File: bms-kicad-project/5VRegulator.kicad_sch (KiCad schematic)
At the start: 45 parts, among them U6 SIC461ED-T1-GE3

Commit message: feat: schematic pretty much done
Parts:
- removed R111: 0, FixedWing:RC1206N_YAG, symbol FixedWing:RC1206JR-070RL
- added R111: 0, FixedWing:RES_CRCW_0805_VIS, symbol FixedWing:CRCW08050000Z0EA
- added TP16, TP17, TP18: TestPoint, TestPoint:TestPoint_Pad_D1.5mm, symbol Connector:TestPoint
- C40: value 220u -> 220µ
- C43: value 1u -> 1µ
- C45: value 4.7u -> 4.7µ
- C49, R117, R118: now not fitted
- C51, C52, C53, C54, C55, C56, C57, C58, C59, C60, C61, C62, C63, C64: value 47u -> 47µ
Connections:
- net +5V: now also TP18.1
- net at R104.1, R105.2, U6.3 (EN): now also TP16.1
- net at LED14.2 (A), R108.2, U6.2 (PGOOD): now also TP17.1
- net at C43.1, R108.1, U6.26 (VDD): now also R111.1
- net at U6.18 (ULTRASONIC): now also R111.2
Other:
- moved on the sheet: C40, C41, C42, C43, C44, C45, C46, C47, C48, C50, C51, C52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

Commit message: feat: schematic cleanup, continued layout
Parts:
- R110: value 41.2 -> 41.2k
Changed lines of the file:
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@@
   (symbol (lib_id "power:GNDA") (at 49.53 240.03 0) (unit 1)
     (in_bom yes) (on_board yes) (dnp no)
-    (property "Reference" "#PWR051" (at 49.53 246.38 0)
+    (property "Reference" "#PWR052" (at 49.53 246.38 0)
       (effects (font (size 1.27 1.27)) hide)
     )
@@
       (project "bms-board"
         (path "/8a7831d1-a913-4f04-8780-225d2234b41d/9bfcf0e7-ef8d-4492-b04a-6397126b0bad"
-          (reference "#PWR051") (unit 1)
+          (reference "#PWR052") (unit 1)
         )
       )
@@
   (symbol (lib_id "power:GNDA") (at 231.14 201.93 0) (unit 1)
     (in_bom yes) (on_board yes) (dnp no)
-    (property "Reference" "#PWR055" (at 231.14 208.28 0)
+    (property "Reference" "#PWR056" (at 231.14 208.28 0)
       (effects (font (size 1.27 1.27)) hide)
     )
@@
       (project "bms-board"
         (path "/8a7831d1-a913-4f04-8780-225d2234b41d/9bfcf0e7-ef8d-4492-b04a-6397126b0bad"
-          (reference "#PWR055") (unit 1)
+          (reference "#PWR056") (unit 1)
         )
       )
@@
   (symbol (lib_id "power:+5V") (at 318.77 50.8 0) (unit 1)
     (in_bom yes) (on_board yes) (dnp no)
-    (property "Reference" "#PWR057" (at 318.77 54.61 0)
+    (property "Reference" "#PWR058" (at 318.77 54.61 0)
       (effects (font (size 1.27 1.27)) hide)
     )
@@
       (project "bms-board"
         (path "/8a7831d1-a913-4f04-8780-225d2234b41d/9bfcf0e7-ef8d-4492-b04a-6397126b0bad"
-          (reference "#PWR057") (unit 1)
+          (reference "#PWR058") (unit 1)
         )
       )
@@
   (symbol (lib_id "power:GNDPWR") (at 236.22 133.35 0) (unit 1)
     (in_bom yes) (on_board yes) (dnp no)
-    (property "Reference" "#PWR056" (at 236.22 138.43 0)
+    (property "Reference" "#PWR057" (at 236.22 138.43 0)
       (effects (font (size 1.27 1.27)) hide)
     )
@@
       (project "bms-board"
         (path "/8a7831d1-a913-4f04-8780-225d2234b41d/9bfcf0e7-ef8d-4492-b04a-6397126b0bad"
-          (reference "#PWR056") (unit 1)
+          (reference "#PWR057") (unit 1)
         )
       )
@@
   (symbol (lib_id "power:GNDPWR") (at 396.24 210.82 0) (unit 1)
     (in_bom yes) (on_board yes) (dnp no) (fields_autoplaced)
-    (property "Reference" "#PWR060" (at 396.24 215.9 0)
+    (property "Reference" "#PWR061" (at 396.24 215.9 0)
       (effects (font (size 1.27 1.27)) hide)
     )
@@
       (project "bms-board"
         (path "/8a7831d1-a913-4f04-8780-225d2234b41d/9bfcf0e7-ef8d-4492-b04a-6397126b0bad"
-          (reference "#PWR060") (unit 1)
+          (reference "#PWR061") (unit 1)
         )
       )
@@
   (symbol (lib_id "power:GNDPWR") (at 44.45 87.63 0) (unit 1)
     (in_bom yes) (on_board yes) (dnp no) (fields_autoplaced)
-    (property "Reference" "#PWR050" (at 44.45 92.71 0)
+    (property "Reference" "#PWR051" (at 44.45 92.71 0)
       (effects (font (size 1.27 1.27)) hide)
     )
@@
       (project "bms-board"
         (path "/8a7831d1-a913-4f04-8780-225d2234b41d/9bfcf0e7-ef8d-4492-b04a-6397126b0bad"
-          (reference "#PWR050") (unit 1)
+          (reference "#PWR051") (unit 1)
         )
       )
@@
   (symbol (lib_id "power:GNDPWR") (at 64.77 240.03 0) (unit 1)
     (in_bom yes) (on_board yes) (dnp no) (fields_autoplaced)
-    (property "Reference" "#PWR052" (at 64.77 245.11 0)
+    (property "Reference" "#PWR053" (at 64.77 245.11 0)
       (effects (font (size 1.27 1.27)) hide)
     )
@@
       (project "bms-board"
         (path "/8a7831d1-a913-4f04-8780-225d2234b41d/9bfcf0e7-ef8d-4492-b04a-6397126b0bad"
-          (reference "#PWR052") (unit 1)
+          (reference "#PWR053") (unit 1)
         )
       )
@@
       (effects (font (size 1.27 1.27)))
     )
-    (property "Value" "41.2" (at 168.91 170.18 0)
+    (property "Value" "41.2k" (at 168.91 170.18 0)
       (effects (font (size 1.27 1.27)))
     )
@@
   (symbol (lib_id "power:+BATT") (at 44.45 67.31 0) (unit 1)
     (in_bom yes) (on_board yes) (dnp no) (fields_autoplaced)
-    (property "Reference" "#PWR049" (at 44.45 71.12 0)
+    (property "Reference" "#PWR050" (at 44.45 71.12 0)
       (effects (font (size 1.27 1.27)) hide)
     )
@@
       (project "bms-board"
         (path "/8a7831d1-a913-4f04-8780-225d2234b41d/9bfcf0e7-ef8d-4492-b04a-6397126b0bad"
-          (reference "#PWR049") (unit 1)
+          (reference "#PWR050") (unit 1)
         )
       )
@@
   (symbol (lib_id "power:GNDPWR") (at 344.17 171.45 0) (unit 1)
     (in_bom yes) (on_board yes) (dnp no)
-    (property "Reference" "#PWR059" (at 344.17 176.53 0)
+    (property "Reference" "#PWR060" (at 344.17 176.53 0)
       (effects (font (size 1.27 1.27)) hide)
     )
@@
       (project "bms-board"
         (path "/8a7831d1-a913-4f04-8780-225d2234b41d/9bfcf0e7-ef8d-4492-b04a-6397126b0bad"
-          (reference "#PWR059") (unit 1)
+          (reference "#PWR060") (unit 1)
         )
       )
@@
   (symbol (lib_id "power:GNDPWR") (at 87.63 102.87 0) (unit 1)
     (in_bom yes) (on_board yes) (dnp no) (fields_autoplaced)
-    (property "Reference" "#PWR054" (at 87.63 107.95 0)
+    (property "Reference" "#PWR055" (at 87.63 107.95 0)
       (effects (font (size 1.27 1.27)) hide)
     )
@@
       (project "bms-board"
         (path "/8a7831d1-a913-4f04-8780-225d2234b41d/9bfcf0e7-ef8d-4492-b04a-6397126b0bad"
-          (reference "#PWR054") (unit 1)
+          (reference "#PWR055") (unit 1)
         )
       )
@@
   (symbol (lib_id "power:GNDPWR") (at 322.58 115.57 0) (unit 1)
     (in_bom yes) (on_board yes) (dnp no) (fields_autoplaced)
-    (property "Reference" "#PWR058" (at 322.58 120.65 0)
+    (property "Reference" "#PWR059" (at 322.58 120.65 0)
       (effects (font (size 1.27 1.27)) hide)
     )
@@
       (project "bms-board"
         (path "/8a7831d1-a913-4f04-8780-225d2234b41d/9bfcf0e7-ef8d-4492-b04a-6397126b0bad"
-          (reference "#PWR058") (unit 1)
+          (reference "#PWR059") (unit 1)
         )
       )
@@
   (symbol (lib_id "power:GND") (at 80.01 240.03 0) (unit 1)
     (in_bom yes) (on_board yes) (dnp no)
-    (property "Reference" "#PWR053" (at 80.01 246.38 0)
+    (property "Reference" "#PWR054" (at 80.01 246.38 0)
       (effects (font (size 1.27 1.27)) hide)
     )
@@
       (project "bms-board"
         (path "/8a7831d1-a913-4f04-8780-225d2234b41d/9bfcf0e7-ef8d-4492-b04a-6397126b0bad"
-          (reference "#PWR053") (unit 1)
-        )
-      )
+          (reference "#PWR054") (unit 1)
+        )
+      )

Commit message: feat: lotta layout
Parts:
- removed LED14: LTST-C170KGKT, FixedWing:LED_LTST-C170KGKT_LTO, symbol FixedWing:LTST-C170KGKT
- removed R108: 10k, FixedWing:KOA_Speer-RK73H2A-0-0-MFG, symbol FixedWing:RK73H2ATTD1002F
- removed R118: R, Resistor_SMD:R_0805_2012Metric, symbol Device:R
- added C41: 0.1µ, FixedWing:CAP_GCJ-18_MUR, symbol FixedWing:GCJ188R72A104KA01D
- added LED15: LTST-C170KGKT, FixedWing:LED_LTST-C170KGKT_LTO, symbol FixedWing:LTST-C170KGKT
- added R109: 93.1k, FixedWing:RESC2012X60N, symbol FixedWing:RC0805FR-0793K1L
- added R116: 5.1k, FixedWing:RESC2012X60N, symbol FixedWing:RC0805JR-075K1L
- renumbered C40 to C39, C41 to C40, R104 to R105, R105 to R106, R106 to R107, R107 to R108, R109 to R110, R110 to R111, R111 to R112, R112 to R113, R113 to R114, R114 to R115, R115 to R117, R116 to R118, R117 to R119, R119 to R120
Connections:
- net +5V: now also R116.2
- net +BATT: now also C41.2
- net GND: now also LED15.1 (K)
- net GNDPWR: now also C41.1
- net PGOOD: now reaches TP17.1, U6.2 (PGOOD)
- net PGOOD: now also R109.2
- net at C43.1, R112.1, U6.26 (VDD): now also R109.1
- new net: LED15.2 (A), R116.1
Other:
- moved on the sheet: C39, C40, C49, R105, R106, R107, R119

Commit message: feat: big pre-design review schematic commit
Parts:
- renumbered C39 to C28, C40 to C29, C41 to C30, C42 to C31, C43 to C32, C44 to C33, C45 to C34, C46 to C35, C47 to C36, C48 to C37, C49 to C38, C50 to C39, C51 to C40, C52 to C41, C53 to C42, C54 to C43, C55 to C44, C56 to C45, C57 to C46, C58 to C47, C59 to C48, C60 to C49, C61 to C50, C62 to C51, C63 to C52, C64 to C53, LED15 to LED13, R110 to R100, R111 to R101, R112 to R102, R113 to R103, R114 to R104, R115 to R105, R116 to R106, R117 to R107, R118 to R108, R119 to R109, R120 to R110, R105 to R95, R106 to R96, R107 to R97, R108 to R98, R109 to R99, TP16 to TP5, TP17 to TP6, TP18 to TP7, U6 to U3
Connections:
- net PGOOD: now also R99.1; no longer R99.2
- net at C32.1, R102.1, U3.26 (VDD): no longer R99.1
- new net +3V3: R99.2
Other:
- company: (none) -> AeroNU - FixedWing
- moved on the sheet: R99

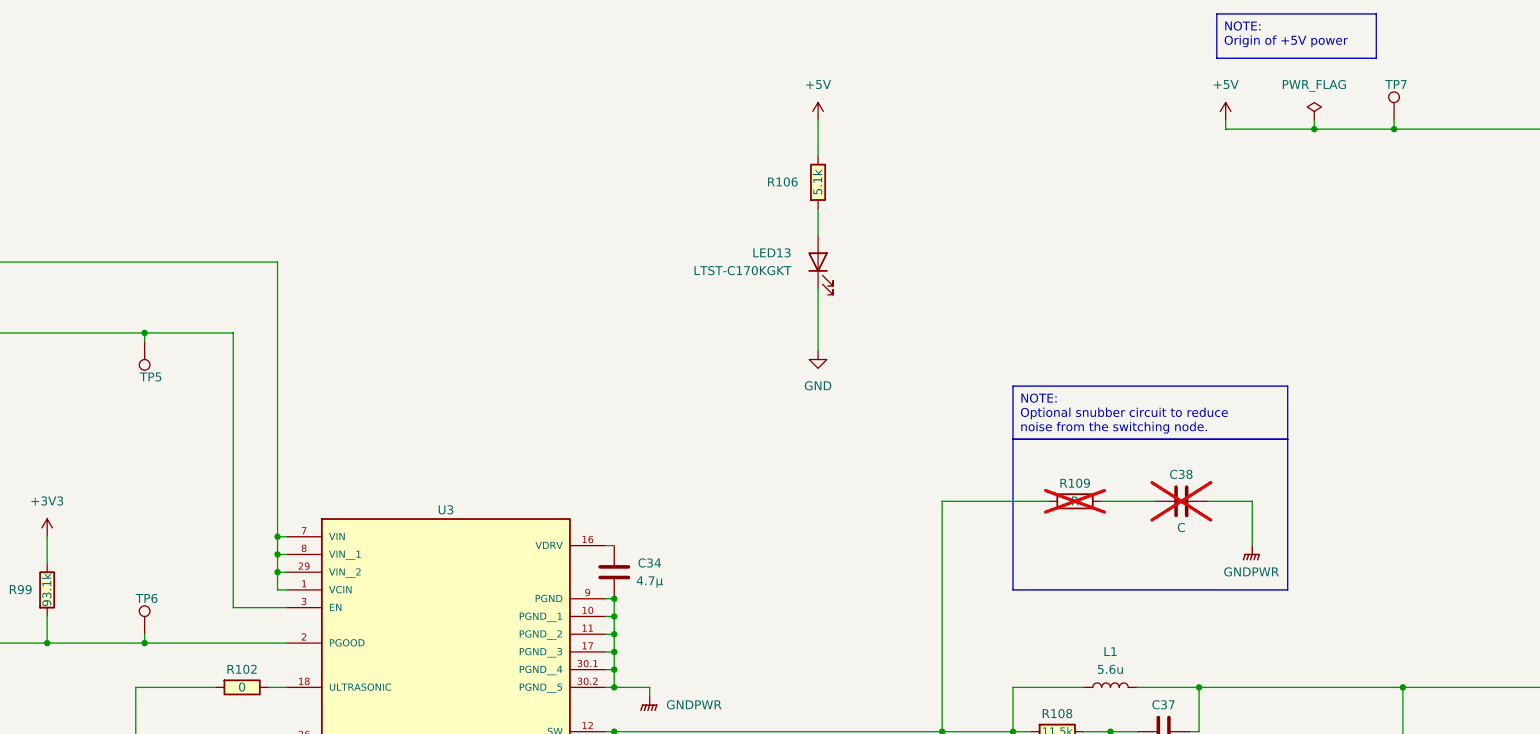
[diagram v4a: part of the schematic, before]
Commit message: feat: post-design review clarity
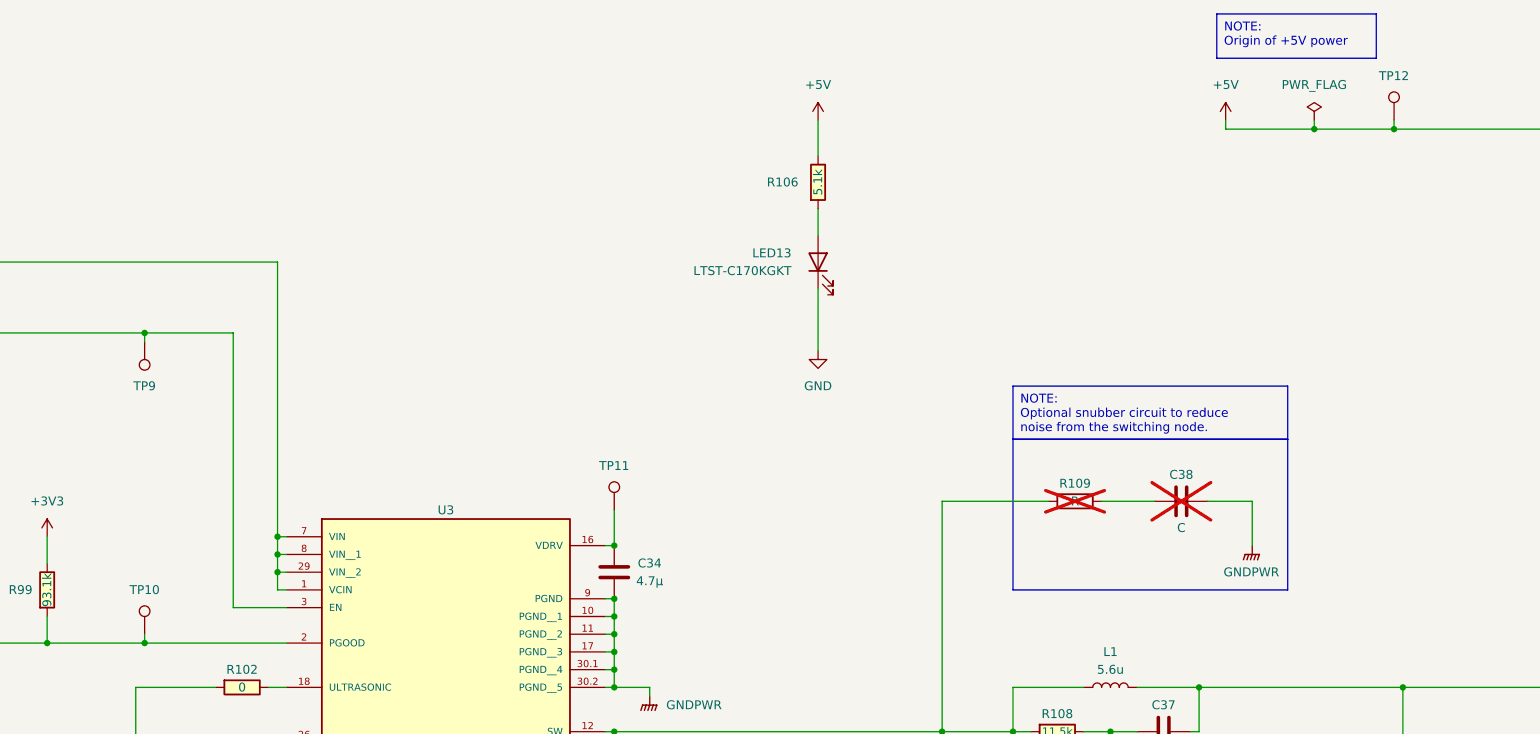
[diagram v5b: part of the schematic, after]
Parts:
- added TP11: ~, TestPoint:TestPoint_Pad_D1.0mm, symbol FixedWing:TestPoint
- TP10: renamed from TP6; value TestPoint -> ~; footprint TestPoint:TestPoint_Pad_D1.5mm -> TestPoint:TestPoint_Pad_D1.0mm; symbol Connector:TestPoint -> FixedWing:TestPoint
- TP12: renamed from TP7; value TestPoint -> ~; footprint TestPoint:TestPoint_Pad_D1.5mm -> TestPoint:TestPoint_Pad_D1.0mm; symbol Connector:TestPoint -> FixedWing:TestPoint
- TP9: renamed from TP5; value TestPoint -> ~; footprint TestPoint:TestPoint_Pad_D1.5mm -> TestPoint:TestPoint_Pad_D1.0mm; symbol Connector:TestPoint -> FixedWing:TestPoint
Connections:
- net at C34.2, U3.16 (VDRV): now also TP11.1

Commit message: feat: I am so tired. 4-layer layout almost done
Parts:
- removed NT2: NetTie_3, NetTie:NetTie-3_SMD_Pad2.0mm, symbol Device:NetTie_3
- removed TP11: ~, TestPoint:TestPoint_Pad_D1.0mm, symbol FixedWing:TestPoint
- added C29, C30, C31: 1µ, FixedWing:CAP_CL31_SAM, symbol FixedWing:CL31B105KCHNNNE
- added C32: 100p, FixedWing:CAPC220145_88N_KEM, symbol FixedWing:C0805C101J1GACTU
- added C58: 47µ, FixedWing:G-32_MUR, symbol FixedWing:GRM32ER71A476KE15L
- added TP6, TP7: 5261, FixedWing:KEYSTONE_5261, symbol FixedWing:5261
- renumbered C29 to C33, C30 to C34, C31 to C35, C32 to C36, C33 to C37, C34 to C38, C35 to C39, C36 to C40, C37 to C41, C38 to C42, C39 to C43, C40 to C44, C41 to C45, C42 to C46, C43 to C47, C44 to C48, C45 to C49, C46 to C50, C47 to C51, C48 to C52, C49 to C53, C50 to C54, C51 to C55, C52 to C56, C53 to C57, TP12 to TP10, TP9 to TP8, TP10 to TP9
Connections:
- net GNDA is gone; now on net GNDPWR: C35.1, C36.2, C37.1, R100.1, R101.1, R104.1, R107.1, U3.23 (AGND), U3.28 (AGND__1)
- net +5V: now also C58.2
- net +BATT: now also C29.2, C30.2, C31.2, C32.2
- net GNDPWR: now also C29.1, C30.1, C31.1, C32.1, C58.1, TP6.TP, TP7.TP
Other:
- moved on the sheet: C28, C33, C34, R95, R96, R97

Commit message: feat: biiig layout and slight design change commit
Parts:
- renumbered C28 to C29, C29 to C30, C30 to C31, C31 to C32, C32 to C33, C33 to C34, C34 to C35, C35 to C36, C36 to C37, C37 to C38, C38 to C39, C39 to C40, C40 to C41, C41 to C42, C42 to C43, C43 to C44, C44 to C45, C45 to C46, C46 to C47, C47 to C48, C48 to C49, C49 to C50, C50 to C51, C51 to C52, C52 to C53, C53 to C54, C54 to C55, C55 to C56, C56 to C57, C57 to C58, C58 to C59, R99 to R100, R100 to R101, R101 to R102, R102 to R103, R103 to R104, R104 to R105, R105 to R106, R106 to R107, R107 to R108, R108 to R109, R109 to R110, R110 to R111, R95 to R96, R96 to R97, R97 to R98, R98 to R99, TP6 to TP5, TP7 to TP6, TP8 to TP7, TP9 to TP8, TP10 to TP9

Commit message: feat:bos->lax layout sesh
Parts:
- removed C43: C, Capacitor_SMD:C_0805_2012Metric, symbol Device:C
- removed R110: R, Resistor_SMD:R_0805_2012Metric, symbol Device:R
- removed TP8: ~, TestPoint:TestPoint_Pad_D1.0mm, symbol FixedWing:TestPoint
- renumbered C44 to C43, C45 to C44, C46 to C45, C47 to C46, C48 to C47, C49 to C48, C50 to C49, C51 to C50, C52 to C51, C53 to C52, C54 to C53, C55 to C54, C56 to C55, C57 to C56, C58 to C57, C59 to C58, R99 to R100, R100 to R101, R101 to R102, R102 to R103, R103 to R104, R104 to R105, R105 to R106, R106 to R107, R107 to R108, R108 to R109, R109 to R110, R96 to R97, R97 to R98, R98 to R99, TP5 to TP3, TP6 to TP4, TP7 to TP5, TP9 to TP6
